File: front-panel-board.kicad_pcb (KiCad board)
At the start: 2 copper layers, 75 x 24 mm, 32 parts, among them J1 Conn_01x05, J10 615108150221R, J11 0532610471, J2 10118193-0001LF, J3 0532610771, J4 0878330821, J5 0532610471, J6 0530480410, J7 Conn_01x03, J8 0532611471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

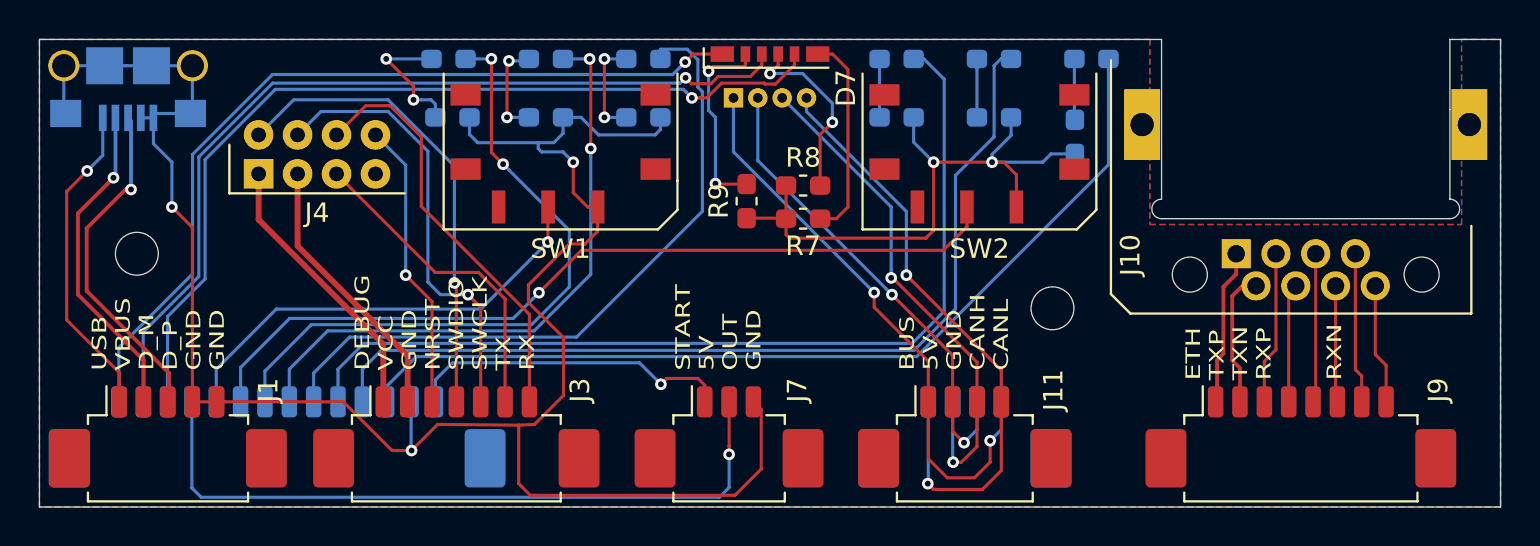
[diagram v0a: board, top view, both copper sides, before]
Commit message: Fixes after PCB review
* Bump trace width to 0.3 mm everywhere (except RJ45 conn)
* Bump clearance to 0.2 mm everywhere (except RJ45 conn)
* Reduced thermal relief width
* Improved ground plane
* Cleaned up USB connector routing / silkscreen
* Moved mechanical elements after review by mechanical engineering.
* Fixed connector labeling
* Bigger traces on CAN connectors for daisy chain

Fixes #1
Fixes #2
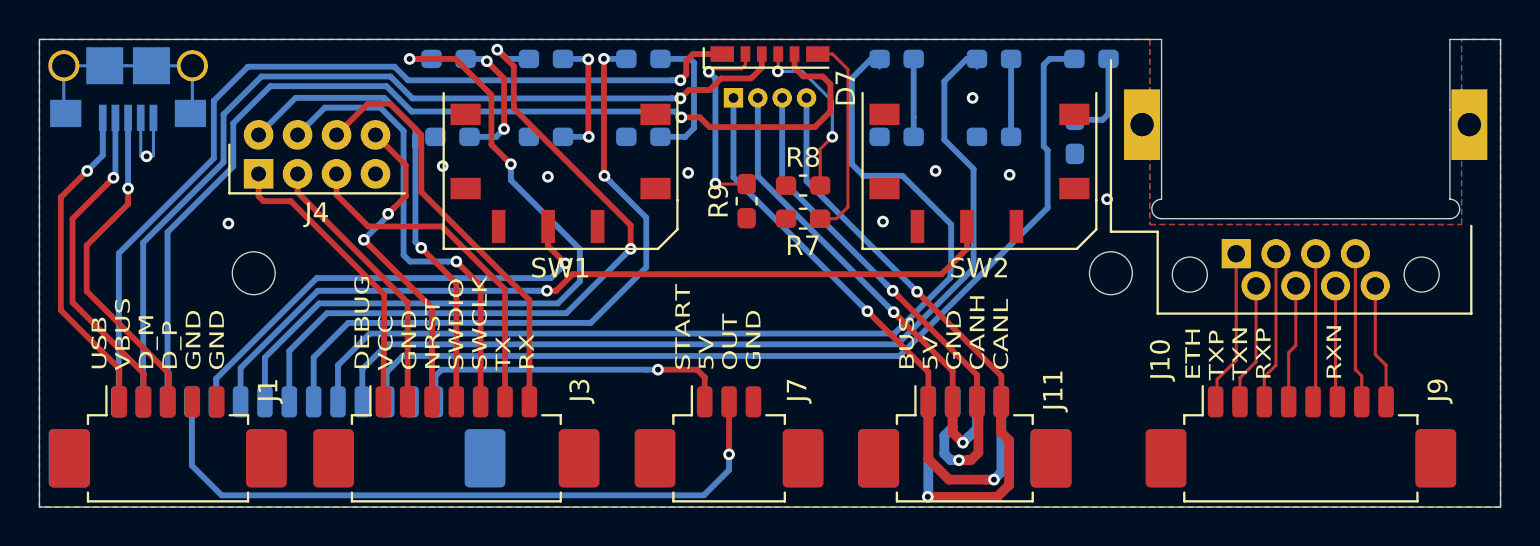
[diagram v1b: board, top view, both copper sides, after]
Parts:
- D1, D2, D3, D4, D5, D6: footprint LED_SMD:LED_0603_1608Metric_Pad1.05x0.95mm_HandSolder -> _LED_SMD:LED_0603_RightAngle
- moved H2 6.08 mm to (136.0, 102.0)
- moved H1 3.50 mm to (180.0, 102.0)
- moved R2 1.00 mm to (174.0, 95.0), turned to 0 degrees
- moved R3 1.00 mm to (151.0, 95.0), turned to 0 degrees
- moved R4 1.00 mm to (169.0, 95.0), turned to 0 degrees
- moved R5 1.00 mm to (156.0, 95.0), turned to 0 degrees
- moved R6 1.00 mm to (146.2, 95.0), turned to 0 degrees
- moved SW1 1.00 mm to (151.8, 95.8)
- moved SW2 1.00 mm to (173.2, 95.8)
- moved G*** 0.25 mm to (161.0, 104.0)
- turned D1 to 180 degrees
- turned D2 to 180 degrees
- turned D3 to 180 degrees
- turned D4 to 180 degrees
- turned D5 to 180 degrees
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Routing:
- net GND: track 135.9 -> 16.2 mm, vias 5 -> 10
- net /LED_TEAM_R: track 46.5 -> 52.6 mm
- net /LED_ERROR: track 31.6 -> 37.2 mm
- net /LED_POWER: track 33.7 -> 37.7 mm
- net /LED_BUS: track 47.9 -> 50.6 mm
- net /LED_TEAM_B: track 43.6 -> 45.6 mm
- net /DEBUG_NRST: track 14.9 -> 16.7 mm, vias 1 -> 2
- net Net-(D5-Pad1): track 5.25 -> 7.07 mm, vias 2 -> 0
- net Net-(J11-Pad4): track 31.8 -> 33.5 mm
- net Net-(D1-Pad1): track 3.17 -> 4.71 mm
- net Net-(D3-Pad1): track 5.13 -> 6.62 mm
- net /LED_COMM: track 35.4 -> 34.0 mm, vias 0 -> 2
- net /LED_TEAM_G: track 45.4 -> 46.7 mm
- net /BUTTON_START: track 36.8 -> 35.5 mm
- net /DEBUG_SWCLK: track 22.8 -> 23.9 mm
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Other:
- net class Default: clearance 0.16 -> 0.2; trace_width 0.16 -> 0.3
- net class Fine added: clearance 0.16, trace_width 0.16, via_dia 0.6, via_drill 0.3
- rule trace_clearance: 0.16 -> 0.2
- board text added: "5V GND D_RDY D_DBG D_BUS D_COM DERR DPW SW1 SW2 START D_R D_G D_B"
- board text added: "M2"
- board text added: "Mounting holes are M2"
- board text removed: "5V GND D_RDY D_DBG D_BUS D_COM D_ERR D_PWR SW1 SW2 START D_B D_G D_R"

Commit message: Minor fixes
* Add a CVRA logo in copper
* Move around some tracks
* Make more tracks 0.3mm
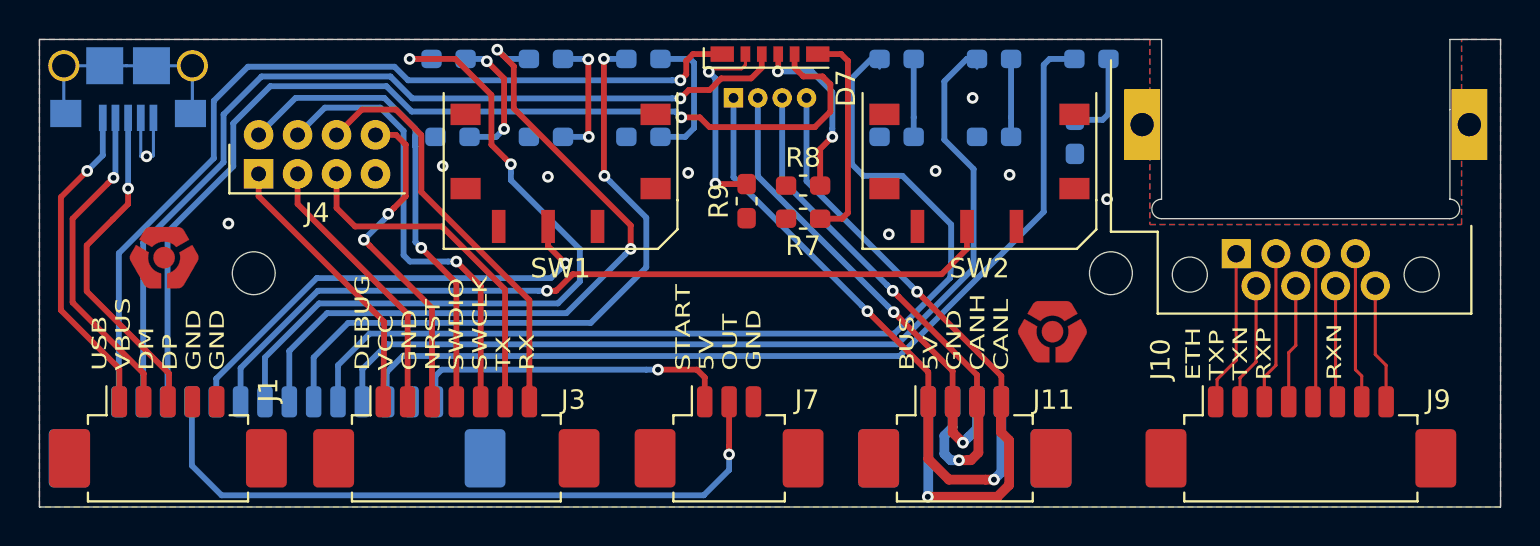
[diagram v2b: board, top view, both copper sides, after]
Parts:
- added G***: LOGO, cvralogo:CVRA-logo-small-copper, F.Cu at (131.4, 101.2)
- added G***: LOGO, cvralogo:CVRA-logo-small-copper, F.Cu at (177.0, 105.0)
- turned G*** to 180 degrees
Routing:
- net /DEBUG_VCC: track 15.2 -> 14.4 mm
- net /DEBUG_NRST: track 16.7 -> 17.3 mm
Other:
- board text added: "5V GND DRDY DDBG DBUS DCOM DERR DPW SW1 SW2 START DR DG DB"
- board text added: "USB VBUS DM DP GND GND"
- board text removed: "5V GND D_RDY D_DBG D_BUS D_COM DERR DPW SW1 SW2 START D_R D_G D_B"
- board text removed: "USB VBUS D_M D_P GND GND"
